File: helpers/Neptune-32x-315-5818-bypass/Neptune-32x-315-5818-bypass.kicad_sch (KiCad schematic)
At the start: 1 part, among them IC504 315-5818

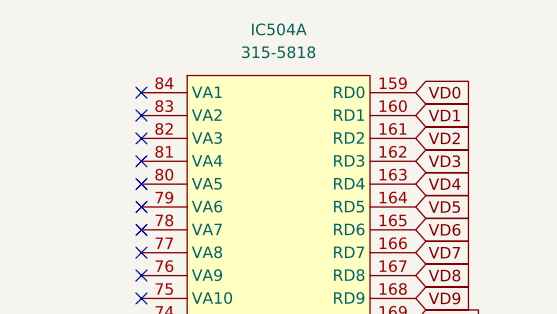
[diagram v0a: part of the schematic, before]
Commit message: Update bypass flexes for 315-5805 and 315-5818 for better connection (issue #11).
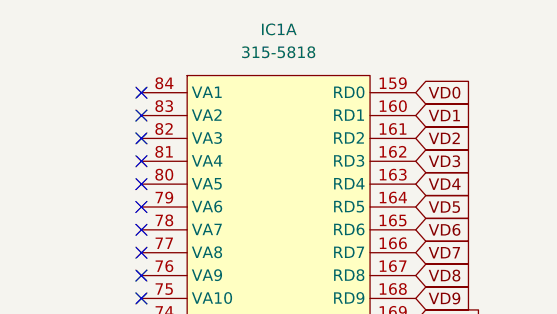
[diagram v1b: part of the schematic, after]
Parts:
- renumbered IC504 to IC1
